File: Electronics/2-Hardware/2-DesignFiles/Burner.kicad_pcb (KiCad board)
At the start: 2 copper layers, 39.4 x 22.9 mm, 16 parts, among them P1 CONN_2, P2 CONN_2, P3 CONN_1, P4 CONN_2, P5 CONN_2, P6 CONN_1, Q1 MOSFET_N, U1 LM317-4PIN, U2 MSP430G2553-20, U3 DIFF_RX

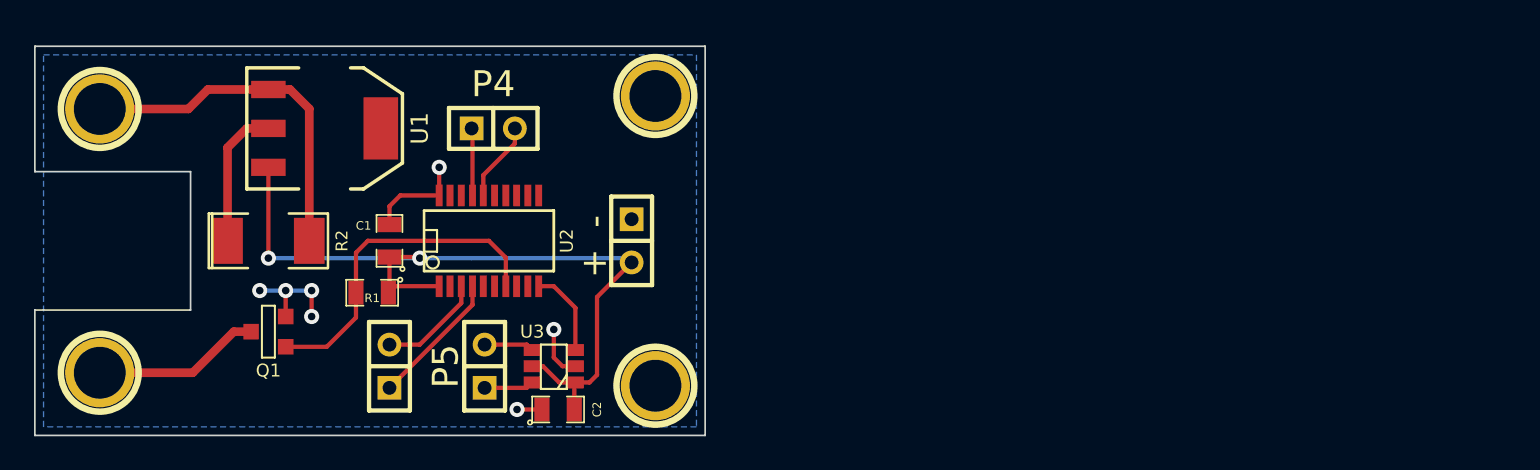
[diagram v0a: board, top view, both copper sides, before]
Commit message: Updated schematic with LEDs, created board layout
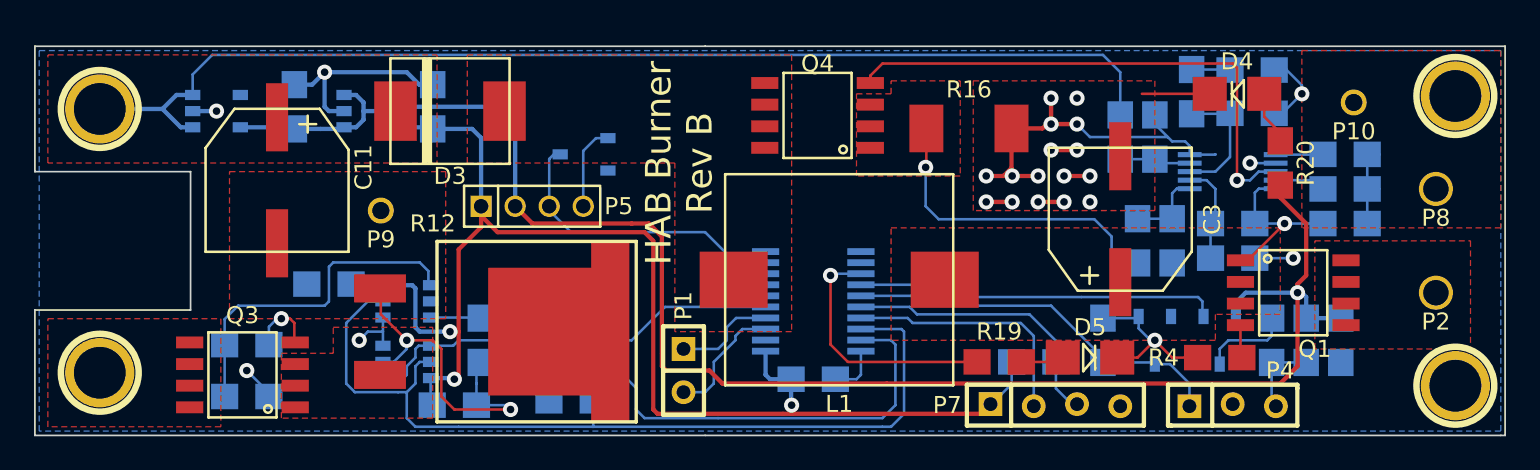
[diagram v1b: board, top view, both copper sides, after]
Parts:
- added C10: 10n, SMD:SMD_0805, B.Cu at (218.4, 169.9)
- added C11: 390u, Capacitors:SMD_POL_E12_8.3mm, F.Cu at (165.9, 166.4)
- added C12: 10u, SMD:SMD_0805, B.Cu at (166.9, 162.1)
- added C13: 10u, SMD:SMD_0805, B.Cu at (175.0, 162.1)
- added C14: 1uF, SMD:SMD_0805, B.Cu at (228.3, 175.8)
- added C3: 390u, Capacitors:SMD_POL_E12_8.3mm, F.Cu at (215.4, 168.7)
- added C4: 0.1uF, SMD:SMD_0805, B.Cu at (168.9, 172.5)
- added C5: 1u, SMD:SMD_0805, B.Cu at (228.6, 168.9)
- added C6: 2.2n, SMD:SMD_0805, B.Cu at (223.1, 162.4)
- added C7: 47n, SMD:SMD_0805, B.Cu at (219.6, 161.2)
- added C8: 0.1uF, SMD:SMD_0805, B.Cu at (176.3, 179.6)
- added C9: 470n, SMD:SMD_0805, B.Cu at (228.6, 166.9)
- added D1: 3V, Diodes:DIODE_SOT-23-3, B.Cu at (217.4, 175.8)
- added D2: 3V, Diodes:DIODE_SOT-23-3, B.Cu at (183.9, 164.8)
- added D3: SL42-E3, Diodes:DIODE_DO214AB-SMC, F.Cu at (176.0, 162.3)
- added D4: D_LED, LEDs:LED_1206, F.Cu at (222.2, 161.3)
- added D5: D_LED, LEDs:LED_1206, F.Cu at (213.6, 176.8)
- added L1: 1.8u, Inductors:IND_BOURNS_SRP1238A, F.Cu at (198.9, 172.2)
- added P10: CONN_1, Connectors:CONN_2.54mm_1x1, F.Cu at (229.1, 161.8)
- added P7: CONN_4, Connectors:CONN_2.54mm_1x4, F.Cu at (211.6, 179.6)
- added P8: CONN_1, Connectors:CONN_2.54mm_1x1, F.Cu at (233.9, 166.9)
- added P9: CONN_1, Connectors:CONN_2.54mm_1x1, F.Cu at (172.0, 168.1)
- added Q2: IRLML6402, Transistors:TRANS_SOT-23-3, B.Cu at (221.2, 175.8)
- added Q3: IRL6342, Transistors:TRANS_SO_4.0mm_1.27mm_8, F.Cu at (163.8, 177.8)
- added Q4: IRF6201, Transistors:TRANS_SO_4.0mm_1.27mm_8, F.Cu at (197.6, 162.6)
- added R10: 41.2k, SMD:SMD_0805, B.Cu at (222.0, 168.9)
- added R11: 45.3k, SMD:SMD_0805, B.Cu at (222.0, 170.9)
- added R12: 1, Resistors:RES_D2PACK, F.Cu at (175.3, 175.3)
- added R13: 8.45k, SMD:SMD_0805, B.Cu at (215.4, 163.8)
- added R14: 40.2k, SMD:SMD_0805, B.Cu at (228.6, 164.8)
- added R15: 100, SMD:SMD_0805, B.Cu at (216.4, 169.9)
- added R16: 3m, SMD:SMD_2010, F.Cu at (206.5, 163.3)
- added R17: 10k, SMD:SMD_0805, B.Cu at (183.1, 179.3)
- added R18: 10k, SMD:SMD_0805, B.Cu at (210.3, 177.0)
- added R19: RES, SMD:SMD_0805, F.Cu at (208.3, 177.0)
- added R20: RES, SMD:SMD_0805, F.Cu at (224.8, 165.4)
- added R3: 100, SMD:SMD_0805, B.Cu at (214.4, 175.8)
- added R4: 10k, SMD:SMD_0805, F.Cu at (221.2, 176.8)
- added R5: 240, SMD:SMD_0805, B.Cu at (224.3, 175.8)
- added R6: 400, SMD:SMD_0805, B.Cu at (226.3, 175.8)
- added R7: 3.16k, SMD:SMD_0805, B.Cu at (223.1, 159.9)
- added R8: 1k, SMD:SMD_0805, B.Cu at (164.1, 176.0)
- added R9: 1k, SMD:SMD_0805, B.Cu at (217.4, 163.8)
- added U4: ADA4805-1, SMD:SOT-23-6, B.Cu at (173.5, 177.0)
- added U5: MIC5203-5.0, SMD:SOT-23-5, B.Cu at (162.3, 162.3)
- added U6: MIC5203-3.3, SMD:SOT-23-5, B.Cu at (171.2, 162.3)
- C1: value 1uF -> 0.1uF; footprint SM0805 -> SMD:SMD_0805; moved to B.Cu
- C2, R1: footprint SM0805 -> SMD:SMD_0805; moved to B.Cu
- P1: footprint CONN_1x2 -> Connectors:CONN_2.54mm_1x2
- P2: value CONN_2 -> CONN_1; footprint CONN_1x2 -> Connectors:CONN_2.54mm_1x1
- P4: value CONN_2 -> CONN_01X03; footprint CONN_1x2 -> Connectors:CONN_2.54mm_1x3
- P5: value CONN_2 -> CONN_01X04; footprint CONN_1x2 -> Connectors:CONN_2.00mm_1x4
- Q1: value MOSFET_N -> IRF9310; footprint SOT23GDS -> Transistors:TRANS_SO_4.0mm_1.27mm_8
- R2: value 2.7 -> 1.6k; footprint SM2010 -> SMD:SMD_0805; moved to B.Cu
- U1: value LM317-4PIN -> ADA4805-1; footprint SOT223 -> SMD:SOT-23-6; moved to B.Cu
- U2: footprint SSOP20 -> SMD:SOP_4.5mm_0.65mm_20; moved to B.Cu
- U3: value DIFF_RX -> LM3481; footprint SOT23_6 -> SMD:SOP_3.0mm_0.5mm_10; moved to B.Cu
- moved Q1 60.2 mm to (225.6, 173.0)
- moved P2 47.3 mm to (233.9, 173.0), turned to 0 degrees
- moved 1PIN 47.0 mm to (235.1, 161.4)
- moved 1PIN 47.0 mm to (235.1, 178.4)
- moved P4 46.4 mm to (222.0, 179.6)
- moved U3 41.5 mm to (222.0, 165.9)
- moved C1 26.2 mm to (197.4, 178.1), turned to 270 degrees
- moved U2 19.4 mm to (197.4, 173.5), turned to 90 degrees
- moved P1 17.3 mm to (189.7, 177.5), turned to 90 degrees
- moved R2 15.6 mm to (179.8, 175.8)
- moved U1 11.2 mm to (173.5, 173.5), turned to 90 degrees
- moved P5 9.80 mm to (180.8, 167.9), turned to 0 degrees
- moved R1 9.56 mm to (164.1, 179.1), turned to 270 degrees
- moved C2 6.12 mm to (177.8, 175.8), turned to 180 degrees
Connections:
- C1 pad 1: +BATT -> +3.3V
- C2 pad 1: GND -> Net-(C2-Pad1)
- C2 pad 2: +BATT -> GND
- P2 pad 1: GND -> Net-(P2-Pad1)
- P3 pad 1: /Ni_+ -> +12V
- P4 pad 1: N-000007 -> /DATA_IN
- P4 pad 2: N-000001 -> GND
- P5 pad 1: N-000002 -> +3.3V
- P5 pad 2: N-000003 -> +5V
- Q1 pad D: /NI_- -> Net-(P2-Pad1)
- Q1 pad G: /MOS_TRIG -> Net-(Q1-PadG)
- Q1 pad S: GND -> Net-(C3-PadP)
- R1 pad 1: +BATT -> Net-(R1-Pad1)
- R1 pad 2: /MOS_TRIG -> GND
- R2 pad 1: /NI_Out -> /PWM
- R2 pad 2: /Ni_+ -> Net-(C2-Pad1)
- U1 pad 1: /Ni_+ -> Net-(R1-Pad1)
- U1 pad 2: /NI_Out -> GND
- U1 pad 3: +BATT -> Net-(C2-Pad1)
- U1 pad 4: (no net) -> Net-(Q3-PadS)
- U2 pad 1: +BATT -> +3.3V
- U2 pad 10: /DATA_IN -> Net-(U2-Pad10)
- U2 pad 11: (no net) -> Net-(U2-Pad11)
- U2 pad 12: (no net) -> Net-(U2-Pad12)
- U2 pad 13: (no net) -> Net-(R19-Pad2)
- U2 pad 14: (no net) -> /DATA_OUT
- U2 pad 15: (no net) -> /DATA_IN
- U2 pad 16: N-000001 -> Net-(P7-Pad3)
- U2 pad 17: N-000007 -> Net-(P7-Pad2)
- U2 pad 18: (no net) -> /OP_CTRL
- U2 pad 19: (no net) -> /PWM
- U2 pad 2: (no net) -> Net-(U2-Pad2)
- U2 pad 5: (no net) -> /SENSE
- U2 pad 6: (no net) -> /EXPANSION
- U2 pad 7: /MOS_TRIG -> Net-(U2-Pad7)
- U2 pad 8: (no net) -> Net-(U2-Pad8)
- U2 pad 9: (no net) -> Net-(U2-Pad9)
- U3 pad 1: +BATT -> Net-(C10-Pad1)
- U3 pad 2: GND -> Net-(R10-Pad2)
- U3 pad 3: /DATA_IN -> Net-(C6-Pad2)
- U3 pad 4: N-000003 -> Net-(R13-Pad1)
- U3 pad 5: +BATT -> GND
- U3 pad 6: N-000002 -> Net-(R14-Pad1)
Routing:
- net +5V: track 0.00 -> 99.4 mm, vias 0 -> 1
- net GND: track 16.6 -> 113.7 mm, vias 7 -> 25
- net +3.3V: track 0.00 -> 81.9 mm, vias 0 -> 3
- net +12V: track 0.00 -> 67.1 mm
- net /OP_CTRL: track 0.00 -> 53.0 mm
- net +BATT: track 47.2 -> 0.00 mm, vias 2 -> 0
- net Net-(Q4-PadG): track 0.00 -> 31.5 mm, vias 0 -> 1
- net /PWM: track 0.00 -> 30.5 mm
- net /SENSE: track 0.00 -> 24.9 mm
- net /DATA_OUT: track 0.00 -> 21.4 mm
- net /Ni_+: track 21.0 -> 0.00 mm
- net Net-(R1-Pad1): track 0.00 -> 20.2 mm
- net /MOS_TRIG: track 19.8 -> 0.00 mm
- net /EXPANSION: track 0.00 -> 19.8 mm
- net Net-(Q4-PadS): track 0.00 -> 19.0 mm, vias 0 -> 1
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- added copper zone on F.Cu, net +12V
- added copper zone on F.Cu, net /NI_-
- added copper zone on F.Cu, net GND
- added copper zone on F.Cu, net Net-(C3-PadP)
- added copper zone on F.Cu, net Net-(D3-PadA)
- added copper zone on F.Cu, net Net-(P2-Pad1)
- added copper zone on F.Cu, net Net-(Q3-PadS)
- added copper zone on F.Cu, net Net-(Q4-PadS)
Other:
- board size 39.4 x 22.9 mm -> 86.4 x 22.9 mm
- net class Default: clearance 0.254 -> 0.1524; trace_width 0.254 -> 0.1524
- net class Power added: clearance 0.1524, trace_width 0.254, via_dia 0.889, via_drill 0.635
- rule trace_clearance: 0.254 -> 0.1524
- rule trace_min: 0.254 -> 0.1524
- board text added: "HAB Burner Rev B"
- board text removed: "+"
- board text removed: "-"

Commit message: Moved parts to fix zone encroachment
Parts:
- moved R4 1.30 mm to (222.5, 177.0)
- moved C3 0.76 mm to (215.4, 167.9)
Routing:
- net Net-(Q1-PadG): track 1.97 -> 3.27 mm
- net GND: track 113.7 -> 114.2 mm
